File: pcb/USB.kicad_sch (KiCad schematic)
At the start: 103 parts, among them J0 12401598E4#2A, J2 1003-002-01100, J3 1003-002-01100, J4 12401598E4#2A, J5 12401598E4#2A, U0 USBLC6-2SC6, U10 AP22811AW5-7, U11 PTN5110DHQ, U12 PTN5110THQ, U13 PTN5110THQ, U14 SN74LVC1G08DCKR, U15 CBTL02043ABQ,115, U19 SN74LVC1G08DCKR, U2 USB7216C, U20 AP22811AW5-7, U21 USBLC6-2SC6, U22 AP22811AW5-7, U23 AP22811AW5-7, U3 CBTL02043ABQ,115, U5 USBLC6-2SC6, U6 CBTL02043ABQ,115, U7 USBLC6-2SC6, U8 USBLC6-2SC6, U9 AP22811AW5-7, X1 ECS-3225MV-250-BN-TR

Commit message: work in progress toward 2.0
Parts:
- U11: value PTN5110DHQ -> PTN5110NHQZ
- U12, U13: value PTN5110THQ -> PTN5110NHQZ
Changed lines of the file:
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@@
   (title_block
     (title "Launch")
-    (date "2021-09-13")
-    (rev "1.4")
+    (date "2022-05-09")
+    (rev "pre-2.0")
     (company "System76")
   )
@@
     (in_bom yes) (on_board yes)
     (property "Reference" "U11" (id 0) (at 170.815 239.649 0))
-    (property "Value" "PTN5110DHQ" (id 1) (at 170.815 241.9604 0))
+    (property "Value" "PTN5110NHQZ" (id 1) (at 170.815 241.9604 0))
     (property "Footprint" "launch:QFN-16-1EP_2.6x2.6mm_P0.4mm_EP1.1x1mm" (id 2) (at 171.45 242.57 0)
       (effects (font (size 1.27 1.27)) (justify left) hide)
@@
     (in_bom yes) (on_board yes)
     (property "Reference" "U12" (id 0) (at 108.585 239.649 0))
-    (property "Value" "PTN5110THQ" (id 1) (at 108.585 241.9604 0))
+    (property "Value" "PTN5110NHQZ" (id 1) (at 108.585 241.9604 0))
     (property "Footprint" "launch:QFN-16-1EP_2.6x2.6mm_P0.4mm_EP1.1x1mm" (id 2) (at 109.22 242.57 0)
       (effects (font (size 1.27 1.27)) (justify left) hide)
@@
     (in_bom yes) (on_board yes)
     (property "Reference" "U13" (id 0) (at 51.435 239.649 0))
-    (property "Value" "PTN5110THQ" (id 1) (at 51.435 241.9604 0))
+    (property "Value" "PTN5110NHQZ" (id 1) (at 51.435 241.9604 0))
     (property "Footprint" "launch:QFN-16-1EP_2.6x2.6mm_P0.4mm_EP1.1x1mm" (id 2) (at 52.07 242.57 0)
       (effects (font (size 1.27 1.27)) (justify left) hide)

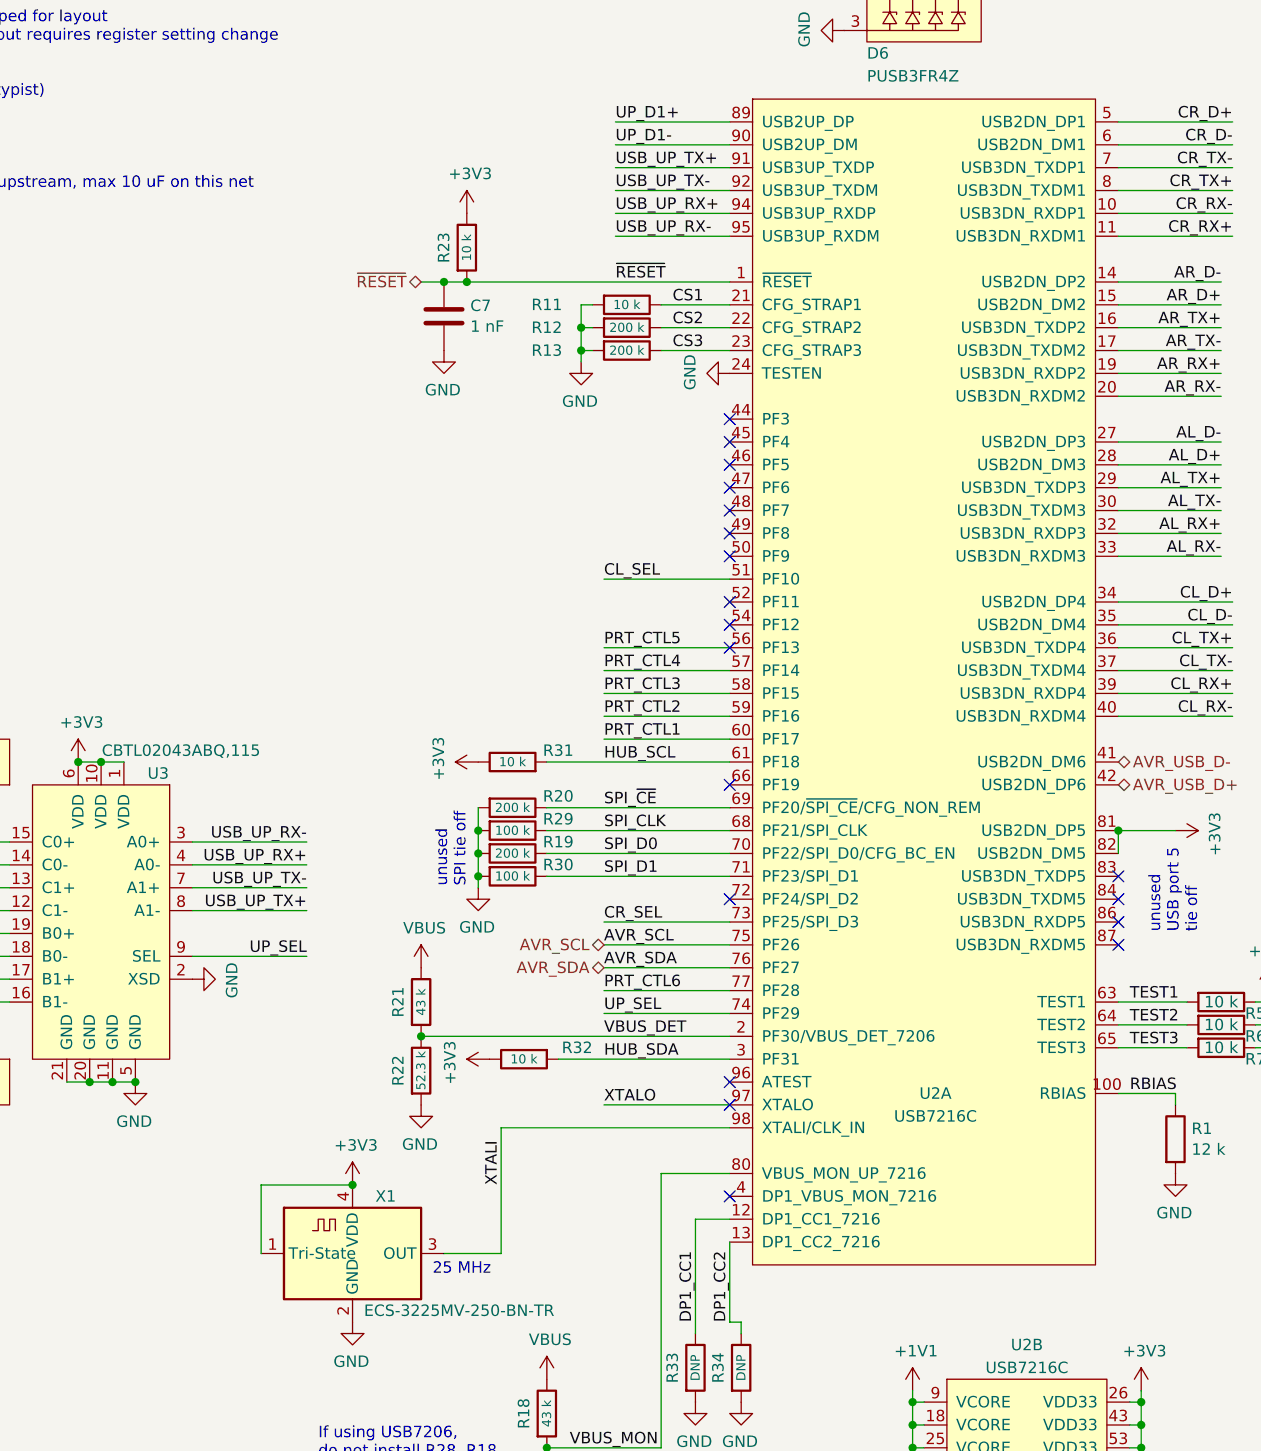
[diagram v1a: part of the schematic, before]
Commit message: version pins, finalize routing FFC connector changed to 20 pin USB hub reset pull down via stitching route remaining nets and cleanup
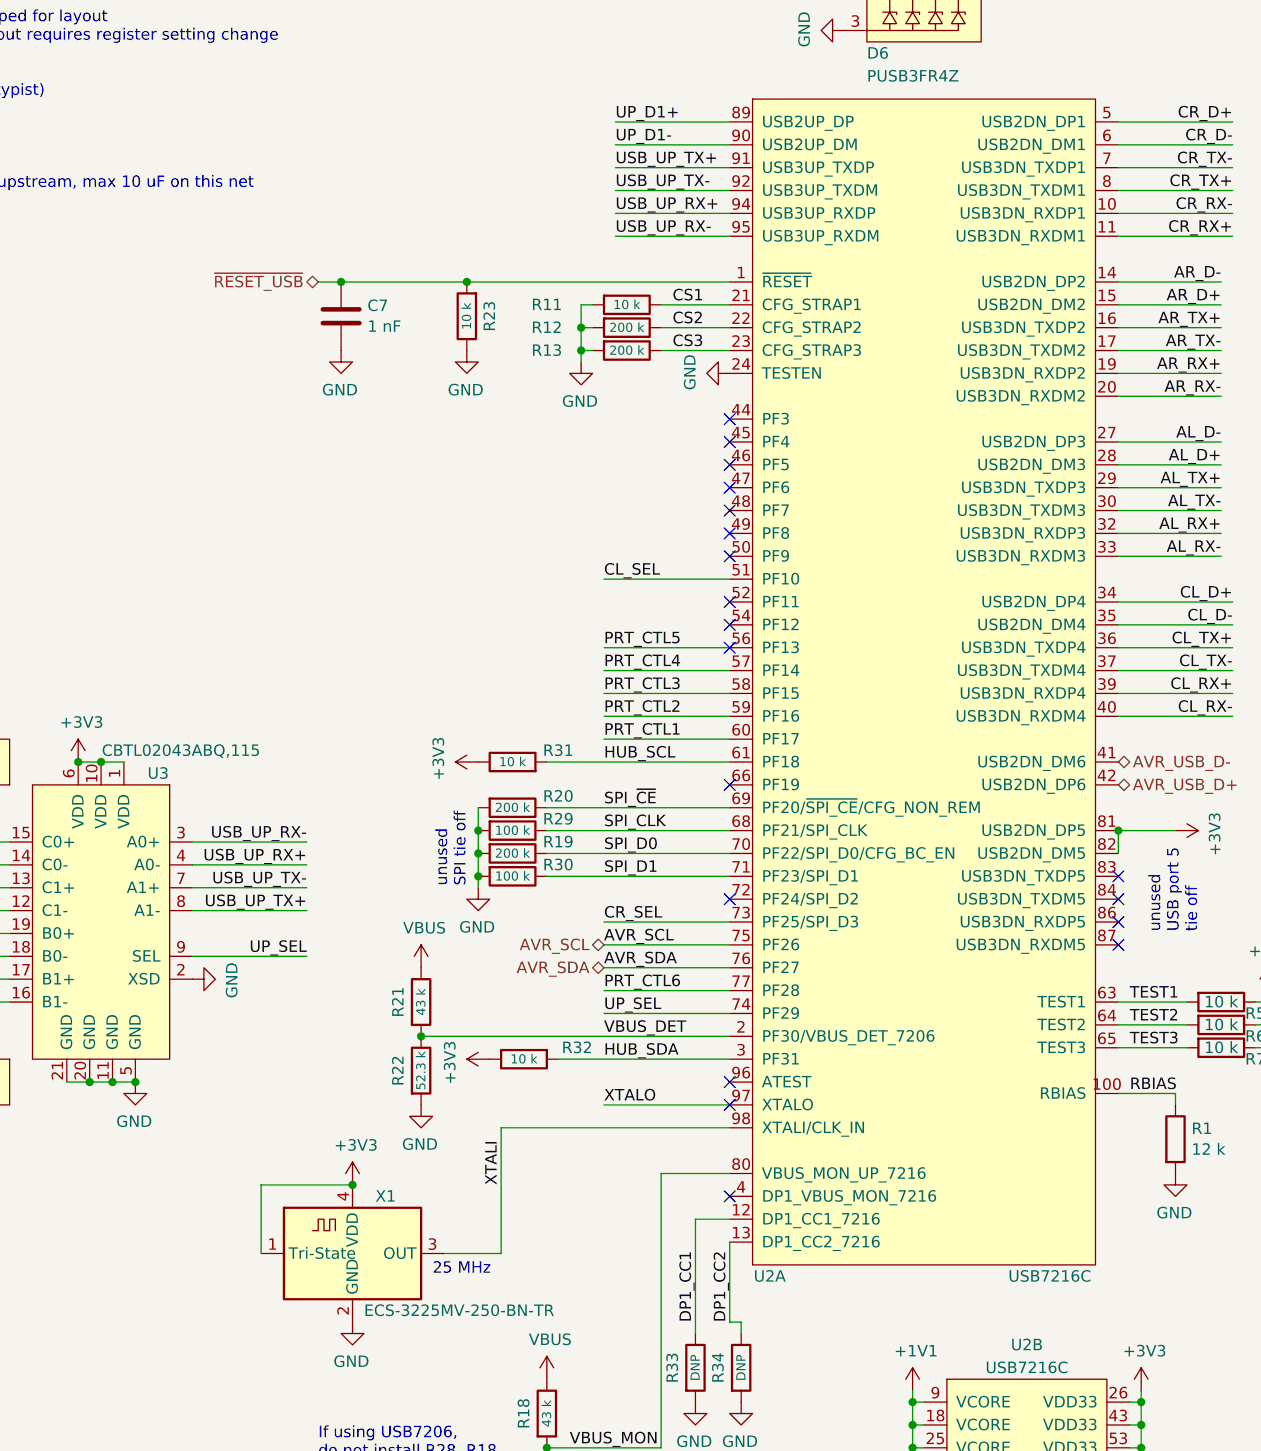
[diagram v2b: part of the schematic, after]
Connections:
- net +3V3: no longer R23.1
- net GND: now also R23.1
- net ~{RESET} renamed ~{RESET_USB}
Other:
- moved on the sheet: C7, R23
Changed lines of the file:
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@@
   (title_block
     (title "Launch")
-    (date "2022-05-09")
+    (date "2022-05-19")
     (rev "pre-2.0")
     (company "System76")
@@
   (junction (at 243.84 269.24) (diameter 0) (color 0 0 0 0)
   )
-  (junction (at 158.75 86.36) (diameter 0) (color 0 0 0 0)
-  )
   (junction (at 146.05 186.69) (diameter 0) (color 0 0 0 0)
   )
@@
   (junction (at 39.37 213.36) (diameter 0) (color 0 0 0 0)
   )
-  (junction (at 156.21 86.36) (diameter 0) (color 0 0 0 0)
+  (junction (at 144.78 86.36) (diameter 0) (color 0 0 0 0)
   )
   (junction (at 328.93 219.71) (diameter 0) (color 0 0 0 0)
@@
   (junction (at 208.28 226.06) (diameter 0) (color 0 0 0 0)
   )
+  (junction (at 158.75 86.36) (diameter 0) (color 0 0 0 0)
+  )
   (junction (at 377.19 87.63) (diameter 0) (color 0 0 0 0)
   )
@@
     (stroke (width 0) (type default) (color 0 0 0 0))
   )
-  (wire (pts (xy 158.75 86.36) (xy 156.21 86.36))
-    (stroke (width 0) (type default) (color 0 0 0 0))
-  )
   (wire (pts (xy 209.55 250.19) (xy 220.98 250.19))
     (stroke (width 0) (type default) (color 0 0 0 0))
@@
     (stroke (width 0) (type default) (color 0 0 0 0))
   )
+  (wire (pts (xy 144.78 86.36) (xy 158.75 86.36))
+    (stroke (width 0) (type default) (color 0 0 0 0))
+  )
   (wire (pts (xy 379.73 99.06) (xy 370.84 99.06))
     (stroke (width 0) (type default) (color 0 0 0 0))
@@
     (stroke (width 0) (type default) (color 0 0 0 0))
   )
+  (wire (pts (xy 158.75 86.36) (xy 187.96 86.36))
+    (stroke (width 0) (type default) (color 0 0 0 0))
+  )
   (wire (pts (xy 328.93 231.14) (xy 328.93 219.71))
     (stroke (width 0) (type default) (color 0 0 0 0))
@@
     (stroke (width 0) (type default) (color 0 0 0 0))
   )
-  (wire (pts (xy 153.67 86.36) (xy 156.21 86.36))
+  (wire (pts (xy 142.24 86.36) (xy 144.78 86.36))
     (stroke (width 0) (type default) (color 0 0 0 0))
   )
@@
     (stroke (width 0) (type default) (color 0 0 0 0))
   )
-  (wire (pts (xy 158.75 86.36) (xy 187.96 86.36))
-    (stroke (width 0) (type default) (color 0 0 0 0))
-  )
   (wire (pts (xy 317.5 118.11) (xy 328.93 118.11))
     (stroke (width 0) (type default) (color 0 0 0 0))
@@
     (effects (font (size 1.27 1.27)) (justify left bottom))
   )
-  (label "~{RESET}" (at 175.26 86.36 0)
-    (effects (font (size 1.27 1.27)) (justify left bottom))
-  )
   (label "PRT_CTL5" (at 173.99 127 0)
     (effects (font (size 1.27 1.27)) (justify left bottom))
@@
     (effects (font (size 1.27 1.27)) (justify right))
   )
-  (hierarchical_label "~{RESET}" (shape bidirectional) (at 153.67 86.36 180)
+  (hierarchical_label "~{RESET_USB}" (shape bidirectional) (at 142.24 86.36 180)
     (effects (font (size 1.27 1.27)) (justify right))
   )
@@
   (symbol (lib_id "launch:USB7206") (at 209.55 121.92 0) (unit 1)
     (in_bom yes) (on_board yes)
-    (property "Reference" "U2" (id 0) (at 210.82 176.53 0))
-    (property "Value" "USB7216C" (id 1) (at 210.82 179.07 0))
+    (property "Reference" "U2" (id 0) (at 192.405 196.85 0))
+    (property "Value" "USB7216C" (id 1) (at 223.52 196.85 0))
     (property "Footprint" "launch:QFN-100-1EP_12x12mm_P0.4mm_EP8x8mm" (id 2) (at 190.5 66.04 0)
       (effects (font (size 1.27 1.27)) hide)
@@
     (pin "1")
   )
-  (symbol (lib_id "Device:R") (at 158.75 82.55 0) (unit 1)
+  (symbol (lib_id "Device:R") (at 158.75 90.17 180) (unit 1)
     (in_bom yes) (on_board yes)
-    (property "Reference" "R23" (id 0) (at 156.21 82.55 90))
-    (property "Value" "10 k" (id 1) (at 158.75 82.55 90)
+    (property "Reference" "R23" (id 0) (at 161.29 90.17 90))
+    (property "Value" "10 k" (id 1) (at 158.75 90.17 90)
       (effects (font (size 1.016 1.016)))
     )
-    (property "Footprint" "launch:R_0402_1005Metric" (id 2) (at 156.972 82.55 90)
+    (property "Footprint" "launch:R_0402_1005Metric" (id 2) (at 160.528 90.17 90)
       (effects (font (size 1.27 1.27)) hide)
     )
-    (property "Datasheet" "~" (id 3) (at 158.75 82.55 0)
+    (property "Datasheet" "~" (id 3) (at 158.75 90.17 0)
       (effects (font (size 1.27 1.27)) hide)
     )
-    (property "Manufacturer" "Generic 1% resistor" (id 4) (at 158.75 82.55 0)
+    (property "Manufacturer" "Generic 1% resistor" (id 4) (at 158.75 90.17 0)
       (effects (font (size 1.27 1.27)) hide)
     )
@@
     (pin "2")
   )
-  (symbol (lib_id "power:+3V3") (at 158.75 78.74 0) (unit 1)
-    (in_bom yes) (on_board yes)
-    (property "Reference" "#PWR0279" (id 0) (at 158.75 82.55 0)
-      (effects (font (size 1.27 1.27)) hide)
-    )
-    (property "Value" "+3V3" (id 1) (at 159.131 74.3458 0))
-    (property "Footprint" "" (id 2) (at 158.75 78.74 0)
-      (effects (font (size 1.27 1.27)) hide)
-    )
-    (property "Datasheet" "" (id 3) (at 158.75 78.74 0)
-      (effects (font (size 1.27 1.27)) hide)
-    )
-    (pin "1")
-  )
   (symbol (lib_id "Device:R") (at 163.83 144.78 270) (unit 1)
     (in_bom yes) (on_board yes)
@@
     (pin "2")
   )
-  (symbol (lib_id "Device:C") (at 156.21 90.17 0) (unit 1)
+  (symbol (lib_id "Device:C") (at 144.78 90.17 0) (unit 1)
     (in_bom yes) (on_board yes)
-    (property "Reference" "C7" (id 0) (at 159.131 89.0016 0)
+    (property "Reference" "C7" (id 0) (at 147.701 89.0016 0)
       (effects (font (size 1.27 1.27)) (justify left))
     )
-    (property "Value" "1 nF" (id 1) (at 159.131 91.313 0)
+    (property "Value" "1 nF" (id 1) (at 147.701 91.313 0)
       (effects (font (size 1.27 1.27)) (justify left))
     )
-    (property "Footprint" "launch:C_0402_1005Metric" (id 2) (at 157.1752 93.98 0)
+    (property "Footprint" "launch:C_0402_1005Metric" (id 2) (at 145.7452 93.98 0)
       (effects (font (size 1.27 1.27)) hide)
     )
-    (property "Datasheet" "~" (id 3) (at 156.21 90.17 0)
+    (property "Datasheet" "~" (id 3) (at 144.78 90.17 0)
       (effects (font (size 1.27 1.27)) hide)
     )
-    (property "Manufacturer" "Generic X7R capacitor" (id 4) (at 156.21 90.17 0)
+    (property "Manufacturer" "Generic X7R capacitor" (id 4) (at 144.78 90.17 0)
       (effects (font (size 1.27 1.27)) hide)
     )
@@
     (pin "2")
   )
-  (symbol (lib_id "power:GND") (at 156.21 93.98 0) (mirror y) (unit 1)
+  (symbol (lib_id "power:GND") (at 144.78 93.98 0) (mirror y) (unit 1)
     (in_bom yes) (on_board yes)
-    (property "Reference" "#PWR0280" (id 0) (at 156.21 100.33 0)
+    (property "Reference" "#PWR0280" (id 0) (at 144.78 100.33 0)
       (effects (font (size 1.27 1.27)) hide)
     )
-    (property "Value" "GND" (id 1) (at 156.083 98.3742 0))
-    (property "Footprint" "" (id 2) (at 156.21 93.98 0)
+    (property "Value" "GND" (id 1) (at 144.653 98.3742 0))
+    (property "Footprint" "" (id 2) (at 144.78 93.98 0)
       (effects (font (size 1.27 1.27)) hide)
     )
-    (property "Datasheet" "" (id 3) (at 156.21 93.98 0)
+    (property "Datasheet" "" (id 3) (at 144.78 93.98 0)
       (effects (font (size 1.27 1.27)) hide)
     )
@@
       (effects (font (size 1.27 1.27)) hide)
     )
+    (pin "1")
+  )
+  (symbol (lib_id "power:GND") (at 158.75 93.98 0) (mirror y) (unit 1)
+    (in_bom yes) (on_board yes)
+    (property "Reference" "#PWR0279" (id 0) (at 158.75 100.33 0)
+      (effects (font (size 1.27 1.27)) hide)
+    )
+    (property "Value" "GND" (id 1) (at 158.623 98.3742 0))
+    (property "Footprint" "" (id 2) (at 158.75 93.98 0)
+      (effects (font (size 1.27 1.27)) hide)
+    )
+    (property "Datasheet" "" (id 3) (at 158.75 93.98 0)
+      (effects (font (size 1.27 1.27)) hide)
+    )

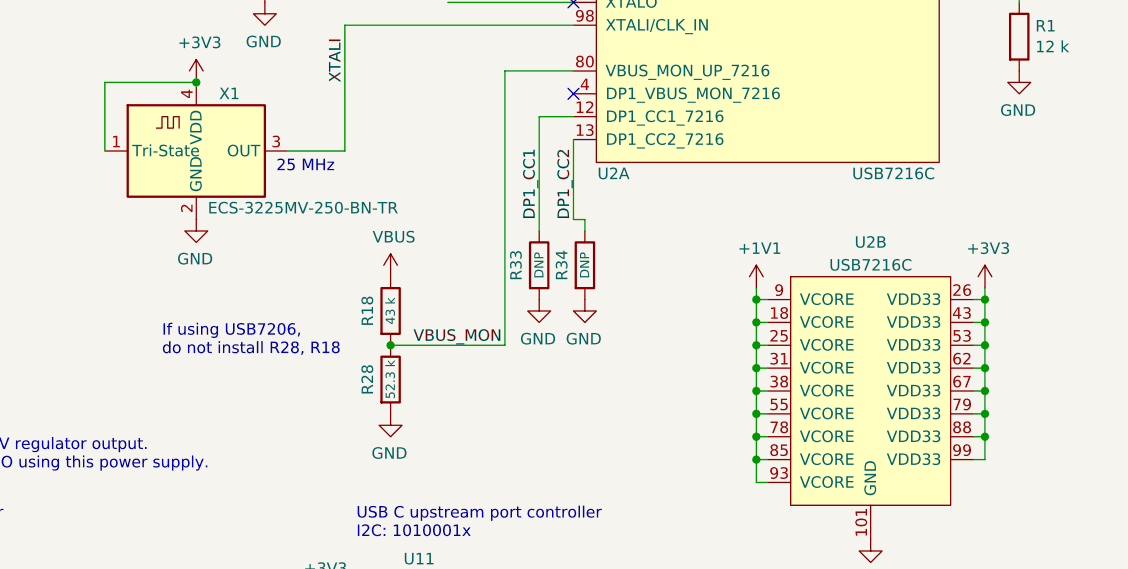
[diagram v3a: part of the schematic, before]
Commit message: change USB7216 to USB7006
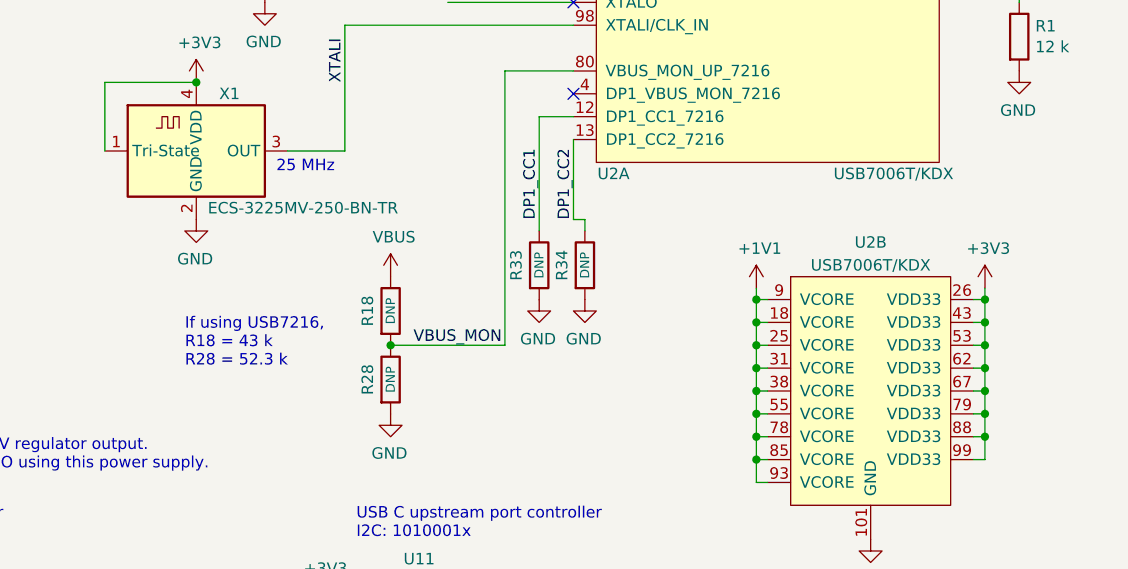
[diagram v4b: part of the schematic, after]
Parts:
- R18: value 43 k -> DNP
- R28: value 52.3 k -> DNP
- U2: value USB7216C -> USB7006T/KDX
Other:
- note added: "If using USB7216, R18 = 43 k R28 = 52.3 k"
- note removed: "If using USB7206, do not install R28, R18"
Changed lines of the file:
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@@
   (title_block
     (title "Launch")
-    (date "2022-05-23")
+    (date "2022-05-24")
     (rev "2.0")
     (company "System76")
@@
     (effects (font (size 1.27 1.27)) (justify left bottom))
   )
-  (text "If using USB7206,\ndo not install R28, R18" (at 142.24 217.17 0)
+  (text "If using USB7216,\nR18 = 43 k\nR28 = 52.3 k" (at 144.78 218.44 0)
     (effects (font (size 1.27 1.27)) (justify left bottom))
   )
@@
     (in_bom yes) (on_board yes)
     (property "Reference" "U2" (id 0) (at 192.405 196.85 0))
-    (property "Value" "USB7216C" (id 1) (at 223.52 196.85 0))
+    (property "Value" "USB7006T/KDX" (id 1) (at 223.52 196.85 0))
     (property "Footprint" "launch:QFN-100-1EP_12x12mm_P0.4mm_EP8x8mm" (id 2) (at 190.5 66.04 0)
       (effects (font (size 1.27 1.27)) hide)
@@
     (in_bom yes) (on_board yes)
     (property "Reference" "U2" (id 0) (at 220.98 204.47 0))
-    (property "Value" "USB7216C" (id 1) (at 220.98 207.01 0))
+    (property "Value" "USB7006T/KDX" (id 1) (at 220.98 207.01 0))
     (property "Footprint" "launch:QFN-100-1EP_12x12mm_P0.4mm_EP8x8mm" (id 2) (at 201.93 165.1 0)
       (effects (font (size 1.27 1.27)) hide)
@@
     (in_bom yes) (on_board yes)
     (property "Reference" "R28" (id 0) (at 165.1 219.71 90))
-    (property "Value" "52.3 k" (id 1) (at 167.64 219.71 90)
+    (property "Value" "DNP" (id 1) (at 167.64 219.71 90)
       (effects (font (size 1.016 1.016)))
     )
@@
     (in_bom yes) (on_board yes)
     (property "Reference" "R18" (id 0) (at 165.1 212.09 90))
-    (property "Value" "43 k" (id 1) (at 167.64 212.09 90)
+    (property "Value" "DNP" (id 1) (at 167.64 212.09 90)
       (effects (font (size 1.016 1.016)))
     )
